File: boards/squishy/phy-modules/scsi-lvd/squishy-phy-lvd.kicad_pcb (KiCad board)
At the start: 6 copper layers, 75 x 55 mm, 22 parts, among them J1 SCSI PHY Mezz, J2 SCSI Connector, U1 M24C02-RMC

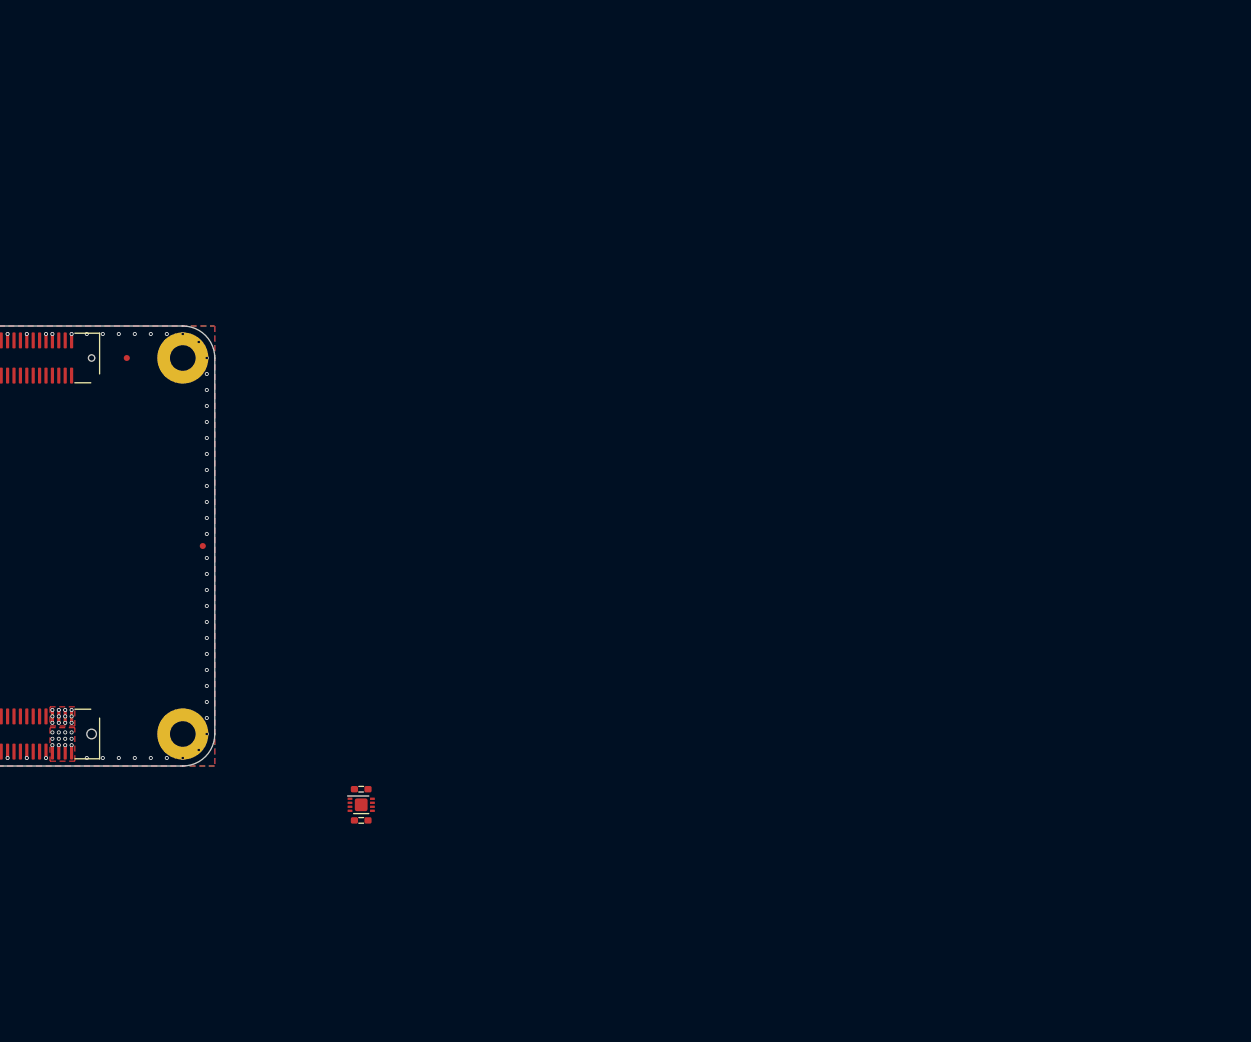
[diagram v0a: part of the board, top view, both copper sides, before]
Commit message: squishy: phy: lvd: Large chunk of work on the LVD phy,
still needs diffsense and termpwr bits implemented and then it can be routed
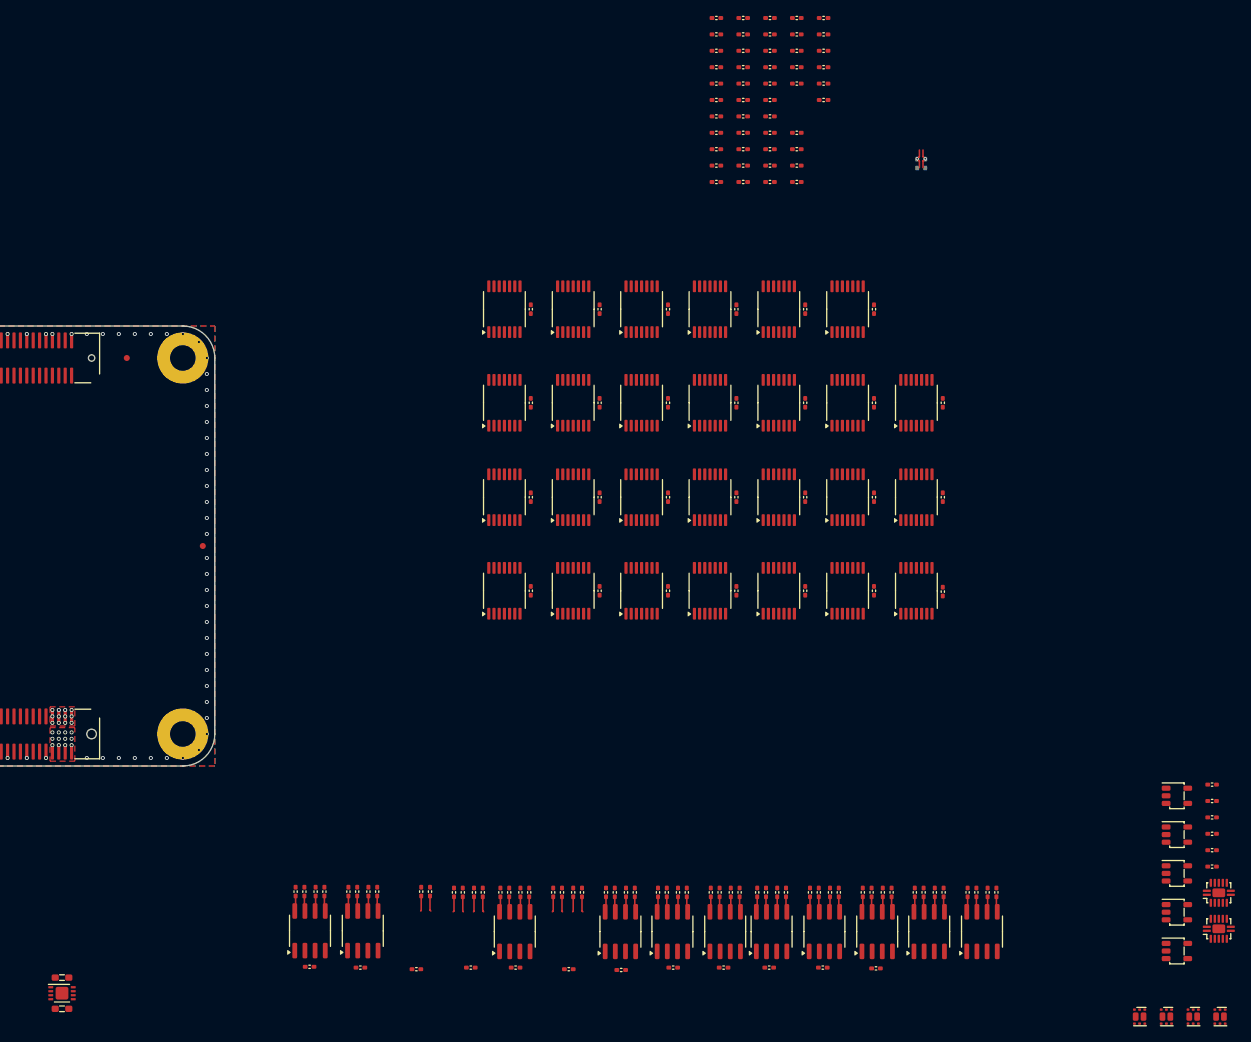
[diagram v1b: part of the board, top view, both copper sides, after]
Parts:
- added C10: 3p, rhais_rcl:C0402, F.Cu at (263.0, 155.8)
- added C100: 1u, rhais_rcl:C0402, F.Cu at (250.2, 82.9)
- added C101: 1u, rhais_rcl:C0402, F.Cu at (258.8, 82.9)
- added C103: 1u, rhais_rcl:C0402, F.Cu at (267.4, 82.9)
- added C106: 1u, rhais_rcl:C0402, F.Cu at (242.3, 165.2)
- added C107: 1u, rhais_rcl:C0402, F.Cu at (248.6, 165.2)
- added C108: 1u, rhais_rcl:C0402, F.Cu at (196.8, 165.1)
- added C109: 1u, rhais_rcl:C0402, F.Cu at (203.2, 165.2)
- added C11: 3p, rhais_rcl:C0402, F.Cu at (259.4, 155.8)
- added C110: 1u, rhais_rcl:C0402, F.Cu at (210.2, 165.4)
- added C111: 1u, rhais_rcl:C0402, F.Cu at (217.0, 165.2)
- added C12: 3p, rhais_rcl:C0402, F.Cu at (260.5, 155.8)
- added C13: 1u, rhais_rcl:C0402, F.Cu at (241.7, 118.1)
- added C14: 1u, rhais_rcl:C0402, F.Cu at (250.2, 118.1)
- added C15: 1u, rhais_rcl:C0402, F.Cu at (261.0, 165.2)
- added C16: 3p, rhais_rcl:C0402, F.Cu at (268.5, 155.8)
- added C17: 3p, rhais_rcl:C0402, F.Cu at (269.6, 155.8)
- added C18: 3p, rhais_rcl:C0402, F.Cu at (266.0, 155.8)
- added C19: 3p, rhais_rcl:C0402, F.Cu at (267.1, 155.8)
- added C2: 3p, rhais_rcl:C0402, F.Cu at (255.3, 155.8)
- added C20: 1u, rhais_rcl:C0402, F.Cu at (258.8, 118.1)
- added C21: 1u, rhais_rcl:C0402, F.Cu at (267.4, 118.1)
- added C22: 1u, rhais_rcl:C0402, F.Cu at (267.6, 165.3)
- added C23: 3p, rhais_rcl:C0402, F.Cu at (275.0, 155.8)
- added C24: 3p, rhais_rcl:C0402, F.Cu at (276.1, 155.8)
- added C25: 3p, rhais_rcl:C0402, F.Cu at (272.5, 155.8)
- added C26: 3p, rhais_rcl:C0402, F.Cu at (273.6, 155.8)
- added C27: 1u, rhais_rcl:C0402, F.Cu at (276.0, 118.2)
- added C28: 1u, rhais_rcl:C0402, F.Cu at (224.5, 106.4)
- added C3: 3p, rhais_rcl:C0402, F.Cu at (256.4, 155.8)
- added C30: 3p, rhais_rcl:C0402, F.Cu at (281.6, 155.8)
- added C31: 3p, rhais_rcl:C0402, F.Cu at (282.7, 155.8)
- added C32: 3p, rhais_rcl:C0402, F.Cu at (279.1, 155.8)
- added C33: 3p, rhais_rcl:C0402, F.Cu at (280.2, 155.8)
- added C34: 1u, rhais_rcl:C0402, F.Cu at (233.1, 106.4)
- added C35: 1u, rhais_rcl:C0402, F.Cu at (241.7, 106.4)
- added C37: 3p, rhais_rcl:C0402, F.Cu at (223.2, 155.8)
- added C38: 3p, rhais_rcl:C0402, F.Cu at (224.3, 155.8)
- added C39: 3p, rhais_rcl:C0402, F.Cu at (220.7, 155.8)
- added C4: 3p, rhais_rcl:C0402, F.Cu at (252.8, 155.8)
- added C40: 3p, rhais_rcl:C0402, F.Cu at (221.8, 155.8)
- added C41: 1u, rhais_rcl:C0402, F.Cu at (250.2, 106.4)
- added C42: 1u, rhais_rcl:C0402, F.Cu at (258.8, 106.4)
- added C43: 1u, rhais_rcl:C0402, F.Cu at (222.6, 165.2)
- added C44: 3p, rhais_rcl:C0402, F.Cu at (229.8, 155.8)
- added C45: 3p, rhais_rcl:C0402, F.Cu at (230.9, 155.8)
- added C46: 3p, rhais_rcl:C0402, F.Cu at (227.3, 155.8)
- added C47: 3p, rhais_rcl:C0402, F.Cu at (228.4, 155.8)
- added C48: 1u, rhais_rcl:C0402, F.Cu at (267.4, 106.4)
- added C49: 1u, rhais_rcl:C0402, F.Cu at (276.0, 106.4)
- added C5: 3p, rhais_rcl:C0402, F.Cu at (253.9, 155.8)
- added C50: 1u, rhais_rcl:C0402, F.Cu at (229.2, 165.4)
- added C51: 3p, rhais_rcl:C0402, F.Cu at (236.4, 155.8)
- added C52: 3p, rhais_rcl:C0402, F.Cu at (237.5, 155.8)
- added C53: 3p, rhais_rcl:C0402, F.Cu at (233.9, 155.8)
- added C54: 3p, rhais_rcl:C0402, F.Cu at (235.0, 155.8)
- added C55: 1u, rhais_rcl:C0402, F.Cu at (224.5, 94.6)
- added C56: 1u, rhais_rcl:C0402, F.Cu at (233.1, 94.6)
- added C57: 1u, rhais_rcl:C0402, F.Cu at (235.8, 165.5)
- added C58: 3p, rhais_rcl:C0402, F.Cu at (242.9, 155.8)
- added C59: 3p, rhais_rcl:C0402, F.Cu at (249.5, 155.8)
- added C6: 1u, rhais_rcl:C0402, F.Cu at (224.5, 118.1)
- added C60: 3p, rhais_rcl:C0402, F.Cu at (197.6, 155.7)
- added C61: 3p, rhais_rcl:C0402, F.Cu at (204.2, 155.7)
- added C62: 3p, rhais_rcl:C0402, F.Cu at (210.8, 155.7)
- added C63: 3p, rhais_rcl:C0402, F.Cu at (217.4, 155.8)
- added C64: 1u, rhais_rcl:C0402, F.Cu at (309.7, 142.3)
- added C65: 1u, rhais_rcl:C0402, F.Cu at (309.7, 144.4)
- added C66: 3p, rhais_rcl:C0402, F.Cu at (244.0, 155.8)
- added C67: 3p, rhais_rcl:C0402, F.Cu at (250.6, 155.8)
- added C68: 3p, rhais_rcl:C0402, F.Cu at (198.7, 155.7)
- added C69: 3p, rhais_rcl:C0402, F.Cu at (205.3, 155.7)
- added C7: 1u, rhais_rcl:C0402, F.Cu at (233.1, 118.1)
- added C70: 3p, rhais_rcl:C0402, F.Cu at (211.9, 155.7)
- added C71: 3p, rhais_rcl:C0402, F.Cu at (218.5, 155.8)
- added C72: 1u, rhais_rcl:C0402, F.Cu at (309.7, 146.4)
- added C73: 1u, rhais_rcl:C0402, F.Cu at (309.7, 148.5)
- added C74: 3p, rhais_rcl:C0402, F.Cu at (240.4, 155.8)
- added C75: 3p, rhais_rcl:C0402, F.Cu at (247.0, 155.8)
- added C76: 3p, rhais_rcl:C0402, F.Cu at (195.1, 155.7)
- added C77: 3p, rhais_rcl:C0402, F.Cu at (201.7, 155.7)
- added C78: 1u, rhais_rcl:C0402, F.Cu at (309.7, 150.5)
- added C79: 3p, rhais_rcl:C0402, F.Cu at (214.9, 155.8)
- added C8: 1u, rhais_rcl:C0402, F.Cu at (254.3, 165.2)
- added C80: 1u, rhais_rcl:C0402, F.Cu at (309.7, 152.6)
- added C82: 3p, rhais_rcl:C0402, F.Cu at (241.5, 155.8)
- added C83: 3p, rhais_rcl:C0402, F.Cu at (248.1, 155.8)
- added C84: 3p, rhais_rcl:C0402, F.Cu at (196.2, 155.7)
- added C85: 3p, rhais_rcl:C0402, F.Cu at (202.8, 155.7)
- added C87: 3p, rhais_rcl:C0402, F.Cu at (216.0, 155.8)
- added C9: 3p, rhais_rcl:C0402, F.Cu at (261.9, 155.8)
- added C90: 1u, rhais_rcl:C0402, F.Cu at (241.7, 94.6)
- added C91: 1u, rhais_rcl:C0402, F.Cu at (250.2, 94.6)
- added C92: 1u, rhais_rcl:C0402, F.Cu at (258.8, 94.6)
- added C93: 1u, rhais_rcl:C0402, F.Cu at (267.4, 94.6)
- added C94: 1u, rhais_rcl:C0402, F.Cu at (276.0, 94.6)
- added C95: 1u, rhais_rcl:C0402, F.Cu at (224.5, 82.9)
- added C98: 1u, rhais_rcl:C0402, F.Cu at (233.1, 82.9)
- added C99: 1u, rhais_rcl:C0402, F.Cu at (241.7, 82.9)
- added Q1: PMDPB58UPE,115, lethalbit-so:SOT1118-3, F.Cu at (300.6, 171.3)
- added Q2: PMDPB58UPE,115, lethalbit-so:SOT1118-3, F.Cu at (303.9, 171.3)
- added Q3: PMDPB58UPE,115, lethalbit-so:SOT1118-3, F.Cu at (307.3, 171.3)
- added Q4: PMDPB58UPE,115, lethalbit-so:SOT1118-3, F.Cu at (310.6, 171.3)
- added R10: 75, rhais_rcl:R0402, F.Cu at (247.7, 62.9)
- added R11: 75, rhais_rcl:R0402, F.Cu at (247.7, 65.0)
- added R12: 75, rhais_rcl:R0402, F.Cu at (247.7, 67.0)
- added R13: 75, rhais_rcl:R0402, F.Cu at (251.1, 46.5)
- added R14: 75, rhais_rcl:R0402, F.Cu at (251.1, 48.5)
- added R15: 75, rhais_rcl:R0402, F.Cu at (251.1, 50.6)
- added R16: 75, rhais_rcl:R0402, F.Cu at (251.1, 52.6)
- added R17: 75, rhais_rcl:R0402, F.Cu at (251.1, 54.7)
- added R18: 75, rhais_rcl:R0402, F.Cu at (251.1, 56.8)
- added R19: 75, rhais_rcl:R0402, F.Cu at (251.1, 58.8)
- added R2: 75, rhais_rcl:R0402, F.Cu at (247.7, 46.5)
- added R20: 75, rhais_rcl:R0402, F.Cu at (251.1, 60.9)
- added R21: 75, rhais_rcl:R0402, F.Cu at (251.1, 62.9)
- added R22: 75, rhais_rcl:R0402, F.Cu at (251.1, 65.0)
- added R23: 75, rhais_rcl:R0402, F.Cu at (251.1, 67.0)
- added R24: 75, rhais_rcl:R0402, F.Cu at (254.4, 46.5)
- added R25: 75, rhais_rcl:R0402, F.Cu at (254.4, 48.5)
- added R26: 75, rhais_rcl:R0402, F.Cu at (254.4, 50.6)
- added R27: 75, rhais_rcl:R0402, F.Cu at (254.4, 52.6)
- added R28: 75, rhais_rcl:R0402, F.Cu at (254.4, 54.7)
- added R29: 75, rhais_rcl:R0402, F.Cu at (254.4, 56.8)
- added R3: 75, rhais_rcl:R0402, F.Cu at (247.7, 48.5)
- added R30: 75, rhais_rcl:R0402, F.Cu at (254.4, 58.8)
- added R31: 75, rhais_rcl:R0402, F.Cu at (254.4, 60.9)
- added R32: 75, rhais_rcl:R0402, F.Cu at (254.4, 62.9)
- added R33: 75, rhais_rcl:R0402, F.Cu at (254.4, 65.0)
- added R34: 75, rhais_rcl:R0402, F.Cu at (254.4, 67.0)
- added R35: 75, rhais_rcl:R0402, F.Cu at (257.8, 46.5)
- added R36: 75, rhais_rcl:R0402, F.Cu at (257.8, 48.5)
- added R37: 75, rhais_rcl:R0402, F.Cu at (257.8, 50.6)
- added R38: 75, rhais_rcl:R0402, F.Cu at (257.8, 52.6)
- added R39: 75, rhais_rcl:R0402, F.Cu at (257.8, 54.7)
- added R4: 75, rhais_rcl:R0402, F.Cu at (247.7, 50.6)
- added R40: 75, rhais_rcl:R0402, B.Cu at (272.8, 64.7)
- added R41: 75, rhais_rcl:R0402, B.Cu at (273.8, 64.7)
- added R42: 75, rhais_rcl:R0402, F.Cu at (257.8, 60.9)
- added R43: 75, rhais_rcl:R0402, F.Cu at (257.8, 62.9)
- added R44: 75, rhais_rcl:R0402, F.Cu at (257.8, 65.0)
- added R45: 75, rhais_rcl:R0402, F.Cu at (257.8, 67.0)
- added R46: 75, rhais_rcl:R0402, F.Cu at (261.1, 46.5)
- added R47: 75, rhais_rcl:R0402, F.Cu at (261.1, 48.5)
- added R48: 75, rhais_rcl:R0402, F.Cu at (261.1, 50.6)
- added R49: 75, rhais_rcl:R0402, F.Cu at (261.1, 52.6)
- added R5: 75, rhais_rcl:R0402, F.Cu at (247.7, 52.6)
- added R50: 75, rhais_rcl:R0402, F.Cu at (261.1, 54.7)
- added R51: 75, rhais_rcl:R0402, F.Cu at (261.1, 56.8)
- added R6: 75, rhais_rcl:R0402, F.Cu at (247.7, 54.7)
- added R7: 75, rhais_rcl:R0402, F.Cu at (247.7, 56.8)
- added R8: 75, rhais_rcl:R0402, F.Cu at (247.7, 58.8)
- added R9: 75, rhais_rcl:R0402, F.Cu at (247.7, 60.9)
- added U10: SN65LVDS180-Q1, Package_SO:TSSOP-14_4.4x5mm_P0.65mm, F.Cu at (264.1, 118.1)
- added U11: SN65LVDS180-Q1, Package_SO:TSSOP-14_4.4x5mm_P0.65mm, F.Cu at (272.7, 118.1)
- added U12: FIN1027A, Package_SO:SOIC-8_3.9x4.9mm_P1.27mm, F.Cu at (274.3, 160.7)
- added U13: SN65LVDS180-Q1, Package_SO:TSSOP-14_4.4x5mm_P0.65mm, F.Cu at (221.2, 106.4)
- added U14: SN65LVDS180-Q1, Package_SO:TSSOP-14_4.4x5mm_P0.65mm, F.Cu at (229.8, 106.4)
- added U15: FIN1027A, Package_SO:SOIC-8_3.9x4.9mm_P1.27mm, F.Cu at (280.9, 160.7)
- added U16: SN65LVDS180-Q1, Package_SO:TSSOP-14_4.4x5mm_P0.65mm, F.Cu at (238.3, 106.4)
- added U17: SN65LVDS180-Q1, Package_SO:TSSOP-14_4.4x5mm_P0.65mm, F.Cu at (246.9, 106.4)
- added U18: FIN1027A, Package_SO:SOIC-8_3.9x4.9mm_P1.27mm, F.Cu at (222.5, 160.7)
- added U19: SN65LVDS180-Q1, Package_SO:TSSOP-14_4.4x5mm_P0.65mm, F.Cu at (255.5, 106.4)
- added U2: SN65LVDS180-Q1, Package_SO:TSSOP-14_4.4x5mm_P0.65mm, F.Cu at (221.2, 118.1)
- added U20: SN65LVDS180-Q1, Package_SO:TSSOP-14_4.4x5mm_P0.65mm, F.Cu at (264.1, 106.4)
- added U22: SN65LVDS180-Q1, Package_SO:TSSOP-14_4.4x5mm_P0.65mm, F.Cu at (272.7, 106.4)
- added U23: SN65LVDS180-Q1, Package_SO:TSSOP-14_4.4x5mm_P0.65mm, F.Cu at (221.2, 94.6)
- added U24: FIN1027A, Package_SO:SOIC-8_3.9x4.9mm_P1.27mm, F.Cu at (235.7, 160.7)
- added U25: SN65LVDS180-Q1, Package_SO:TSSOP-14_4.4x5mm_P0.65mm, F.Cu at (229.8, 94.6)
- added U26: SN65LVDS180-Q1, Package_SO:TSSOP-14_4.4x5mm_P0.65mm, F.Cu at (238.3, 94.6)
- added U27: SN65LVDS180-Q1, Package_SO:TSSOP-14_4.4x5mm_P0.65mm, F.Cu at (246.9, 94.6)
- added U28: SN65LVDS180-Q1, Package_SO:TSSOP-14_4.4x5mm_P0.65mm, F.Cu at (255.5, 94.6)
- added U29: SN65LVDS180-Q1, Package_SO:TSSOP-14_4.4x5mm_P0.65mm, F.Cu at (264.1, 94.6)
- added U3: FIN1027A, Package_SO:SOIC-8_3.9x4.9mm_P1.27mm, F.Cu at (254.6, 160.7)
- added U30: SN65LVDS180-Q1, Package_SO:TSSOP-14_4.4x5mm_P0.65mm, F.Cu at (272.7, 94.6)
- added U31: SN65LVDS180-Q1, Package_SO:TSSOP-14_4.4x5mm_P0.65mm, F.Cu at (221.2, 82.9)
- added U32: ~, rhais_package-qfn:DHVQFN-14-1EP_2.5x3mm_P0.5mm_EP1x1.5mm, F.Cu at (310.5, 155.8)
- added U33: ~, rhais_package-qfn:DHVQFN-14-1EP_2.5x3mm_P0.5mm_EP1x1.5mm, F.Cu at (310.5, 160.3)
- added U34: FIN1027A, Package_SO:SOIC-8_3.9x4.9mm_P1.27mm, F.Cu at (242.2, 160.7)
- added U35: FIN1027A, Package_SO:SOIC-8_3.9x4.9mm_P1.27mm, F.Cu at (248.8, 160.7)
- added U36: FIN1027A, Package_SO:SOIC-8_3.9x4.9mm_P1.27mm, F.Cu at (196.9, 160.6)
- added U37: FIN1027A, Package_SO:SOIC-8_3.9x4.9mm_P1.27mm, F.Cu at (203.5, 160.6)
- added U4: SN65LVDS180-Q1, Package_SO:TSSOP-14_4.4x5mm_P0.65mm, F.Cu at (229.8, 118.1)
- added U40: ~, rhais_package-smd:SOT-23-5, F.Cu at (305.3, 143.7)
- added U41: ~, rhais_package-smd:SOT-23-5, F.Cu at (305.3, 148.6)
- added U42: SN65LVDS180-Q1, Package_SO:TSSOP-14_4.4x5mm_P0.65mm, F.Cu at (229.8, 82.9)
- added U43: SN65LVDS180-Q1, Package_SO:TSSOP-14_4.4x5mm_P0.65mm, F.Cu at (238.3, 82.9)
- added U44: SN65LVDS180-Q1, Package_SO:TSSOP-14_4.4x5mm_P0.65mm, F.Cu at (246.9, 82.9)
- added U45: SN65LVDS180-Q1, Package_SO:TSSOP-14_4.4x5mm_P0.65mm, F.Cu at (255.5, 82.9)
- added U46: ~, rhais_package-smd:SOT-23-5, F.Cu at (305.3, 153.4)
- added U47: SN65LVDS180-Q1, Package_SO:TSSOP-14_4.4x5mm_P0.65mm, F.Cu at (264.1, 82.9)
- added U48: ~, rhais_package-smd:SOT-23-5, F.Cu at (305.3, 158.3)
- added U49: ~, rhais_package-smd:SOT-23-5, F.Cu at (305.3, 163.1)
- added U5: SN65LVDS180-Q1, Package_SO:TSSOP-14_4.4x5mm_P0.65mm, F.Cu at (238.3, 118.1)
- added U6: FIN1027A, Package_SO:SOIC-8_3.9x4.9mm_P1.27mm, F.Cu at (261.2, 160.7)
- added U7: SN65LVDS180-Q1, Package_SO:TSSOP-14_4.4x5mm_P0.65mm, F.Cu at (246.9, 118.1)
- added U8: SN65LVDS180-Q1, Package_SO:TSSOP-14_4.4x5mm_P0.65mm, F.Cu at (255.5, 118.1)
- added U9: FIN1027A, Package_SO:SOIC-8_3.9x4.9mm_P1.27mm, F.Cu at (267.8, 160.7)
- moved U1 44.2 mm to (165.9, 168.4)
- moved C1 44.2 mm to (165.9, 170.3)
- moved R1 44.2 mm to (165.9, 166.4)
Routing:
- net /CON.RST-: track 0.00 -> 2.43 mm, vias 0 -> 1
- net /CON.RST+: track 0.00 -> 2.43 mm, vias 0 -> 1
- net Net-(C79-Pad1): track 0.00 -> 1.92 mm
- net Net-(C74-Pad1): track 0.00 -> 1.92 mm
- net Net-(C68-Pad1): track 0.00 -> 1.92 mm
- net Net-(C67-Pad1): track 0.00 -> 1.92 mm
- net Net-(C53-Pad1): track 0.00 -> 1.92 mm
- net Net-(C46-Pad1): track 0.00 -> 1.92 mm
- net Net-(C4-Pad1): track 0.00 -> 1.92 mm
- net Net-(C32-Pad1): track 0.00 -> 1.92 mm
- net Net-(C31-Pad1): track 0.00 -> 1.92 mm
- net Net-(C3-Pad1): track 0.00 -> 1.92 mm
- net Net-(C25-Pad1): track 0.00 -> 1.92 mm
- net Net-(C18-Pad1): track 0.00 -> 1.92 mm
- net Net-(C10-Pad1): track 0.00 -> 1.92 mm
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
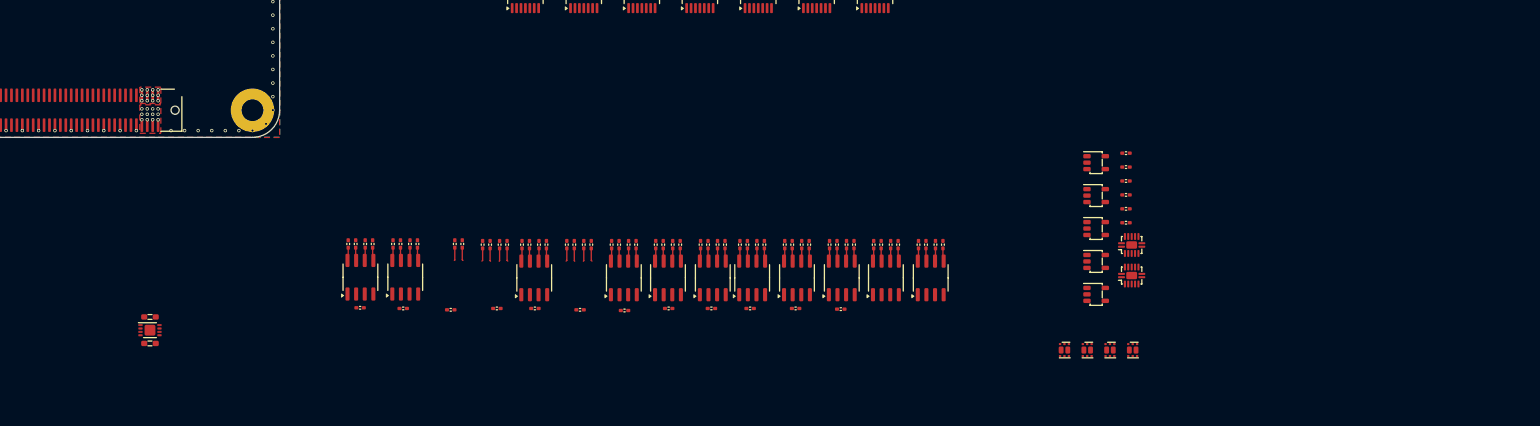
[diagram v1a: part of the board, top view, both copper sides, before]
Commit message: squishy: phy: lvd: updated the PCB with the mostly finished schematic bits.
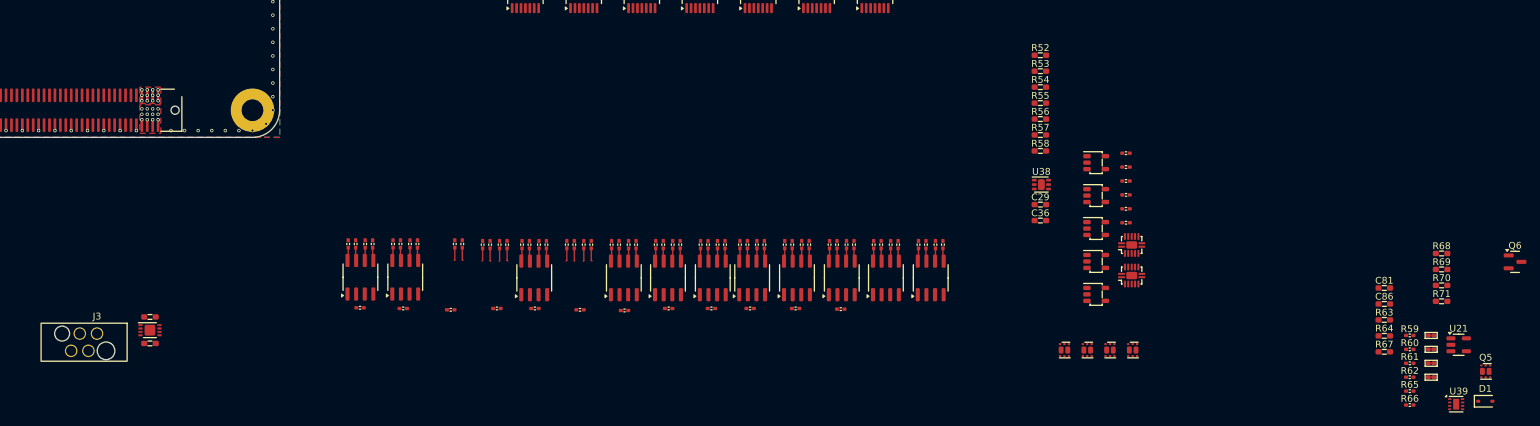
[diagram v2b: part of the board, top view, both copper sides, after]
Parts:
- added C29: 1u, rhais_rcl:C0603, F.Cu at (297.1, 149.9)
- added C36: 1u, rhais_rcl:C0603, F.Cu at (297.1, 152.2)
- added C81: 100n, rhais_rcl:C0603, F.Cu at (347.7, 162.2)
- added C86: 100n, rhais_rcl:C0603, F.Cu at (347.7, 164.5)
- added D1: Vz=2V @ 2%, Diode_SMD:D_SOD-323, F.Cu at (362.6, 178.9)
- added J3: Conn_01x04, pkl_connectors_wuerth:490107670412-d, F.Cu at (158.1, 168.9)
- added JP1: PWR_JMPR, pkl_jumpers:J_NC_0402_30, F.Cu at (354.6, 169.2)
- added JP2: PWR_JMPR, pkl_jumpers:J_NC_0402_30, F.Cu at (354.6, 171.2)
- added JP3: PWR_JMPR, pkl_jumpers:J_NC_0402_30, F.Cu at (354.6, 173.3)
- added JP4: PWR_JMPR, pkl_jumpers:J_NC_0402_30, F.Cu at (354.6, 175.3)
- added Q5: PMDPB58UPE,115, lethalbit-so:SOT1118-3, F.Cu at (362.7, 174.5)
- added Q6: DMN65D8L-7, Package_TO_SOT_SMD:SOT-23, F.Cu at (367.0, 158.3)
- added R52: 10k, rhais_rcl:R0603, F.Cu at (297.1, 127.9)
- added R53: 10k, rhais_rcl:R0603, F.Cu at (297.1, 130.2)
- added R54: 10k, rhais_rcl:R0603, F.Cu at (297.1, 132.6)
- added R55: 10k, rhais_rcl:R0603, F.Cu at (297.1, 134.9)
- added R56: 10k, rhais_rcl:R0603, F.Cu at (297.1, 137.3)
- added R57: 10k, rhais_rcl:R0603, F.Cu at (297.1, 139.7)
- added R58: 10k, rhais_rcl:R0603, F.Cu at (297.1, 142.0)
- added R59: 300, rhais_rcl:R0402, F.Cu at (351.5, 169.2)
- added R60: 220k, rhais_rcl:R0402, F.Cu at (351.5, 171.2)
- added R61: 220k, rhais_rcl:R0402, F.Cu at (351.5, 173.3)
- added R62: 100k, rhais_rcl:R0402, F.Cu at (351.5, 175.3)
- added R63: 10k, rhais_rcl:R0603, F.Cu at (347.7, 166.9)
- added R64: 10k, rhais_rcl:R0603, F.Cu at (347.7, 169.2)
- added R65: 100k, rhais_rcl:R0402, F.Cu at (351.5, 177.4)
- added R66: 175k, rhais_rcl:R0402, F.Cu at (351.5, 179.4)
- added R67: 10k, rhais_rcl:R0603, F.Cu at (347.7, 171.6)
- added R68: 10k, rhais_rcl:R0603, F.Cu at (356.1, 157.1)
- added R69: 10k, rhais_rcl:R0603, F.Cu at (356.1, 159.4)
- added R70: 10k, rhais_rcl:R0603, F.Cu at (356.1, 161.8)
- added R71: 10k, rhais_rcl:R0603, F.Cu at (356.1, 164.2)
- added U21: LM321, Package_TO_SOT_SMD:SOT-23-5, F.Cu at (358.7, 170.6)
- added U38: TLV75512PDRV, rhais_package-qfn:WSON-6-1EP_2x2mm_P0.65mm_EP1x1.6mm, F.Cu at (297.2, 146.9)
- added U39: LM2903, Package_SON:WSON-8-1EP_2x2mm_P0.5mm_EP0.9x1.6mm, F.Cu at (358.3, 179.3)
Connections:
- net /Termination/1v2 renamed /INT_TERMPWR
- J2 pad 3: unconnected-(J2-Pin_3-Pad3) -> +3V3

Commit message: squishy: phy: lvd: Started re-working the LVD PHY
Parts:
- removed R10, R11, R12, R13, R14, R15, R16, R17, R18, R19, R2, R20, R21, R22, R23, R24, R25, R26, R27, R28, R29, R3, R30, R31, R32, R33, R34, R35, R36, R37, R38, R39, R4, R40, R41, R42, R43, R44, R45, R46, R47, R48, R49, R5, R50, R51, R6, R7, R8, R9: 75, rhais_rcl:R0402
- added C88: 4u7, rhais_rcl:C0402, F.Cu at (140.7, 60.3)
- added C89: 4u7, rhais_rcl:C0402, F.Cu at (170.8, 68.2)
- added R74: 100k, rhais_rcl:R0402, F.Cu at (167.0, 72.0)
- added R75: 100k, rhais_rcl:R0402, F.Cu at (167.0, 71.0)
- added U50: UCC5640PW24, Package_SO:TSSOP-24_4.4x7.8mm_P0.65mm, F.Cu at (147.5, 61.5)
- added U51: UCC5640PW24, Package_SO:TSSOP-24_4.4x7.8mm_P0.65mm, F.Cu at (136.0, 61.5)
- C29, C36: value 1u -> 4u7; footprint rhais_rcl:C0603 -> rhais_rcl:C0402
- U38: value TLV75512PDRV -> UCC5640PW24; footprint rhais_package-qfn:WSON-6-1EP_2x2mm_P0.65mm_EP1x1.6mm -> Package_SO:TSSOP-24_4.4x7.8mm_P0.65mm
- moved C36 171.6 mm to (152.2, 60.3), turned to 90 degrees
- moved U38 162.5 mm to (159.0, 61.5), turned to -90 degrees
- moved C29 160.7 mm to (163.7, 60.3), turned to 90 degrees
- moved U15 145.8 mm to (150.0, 225.0)
- moved C24 139.9 mm to (151.8, 220.0)
- moved C23 139.9 mm to (150.8, 220.0)
- moved U12 133.3 mm to (157.5, 225.0)
- moved C17 123.3 mm to (164.3, 220.0)
- moved C16 123.3 mm to (163.2, 220.0)
- moved U9 121.3 mm to (165.0, 225.0)
- moved C59 119.9 mm to (148.2, 220.0)
- moved C67 119.9 mm to (149.3, 220.0)
- moved C32 113.3 mm to (185.8, 220.1)
- moved C33 113.3 mm to (186.8, 220.1)
- moved C30 113.3 mm to (188.2, 220.0)
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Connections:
- C29 pad 1: /INT_TERMPWR -> GND
- C29 pad 2: GND -> Net-(U38A-REG)
- C36 pad 1: +5V -> GND
- C36 pad 2: GND -> Net-(U50A-REG)
- U38 pad 1: /INT_TERMPWR -> Net-(U38A-REG)
- U38 pad 2: unconnected-(U38-NC-Pad2) -> /CON.DB12+
- U38 pad 3: GND -> /CON.DB12-
- U38 pad 4: /PHY.LS_CTRL5 -> /CON.DB14+
- U38 pad 5: unconnected-(U38-NC-Pad5) -> /CON.DB14-
- U38 pad 6: +5V -> /CON.DP1+
- U38 pad 7: GND -> /CON.DP1-
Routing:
- net /CON.RST-: track 2.43 -> 0.00 mm, vias 1 -> 0
- net /CON.RST+: track 2.43 -> 0.00 mm, vias 1 -> 0
- net Net-(U51A-REG): track 0.00 -> 1.97 mm
- net Net-(U50A-REG): track 0.00 -> 1.97 mm
- net Net-(U38A-REG): track 0.00 -> 1.97 mm
- net Net-(C79-Pad1): track 1.92 -> 0.00 mm
- net Net-(C74-Pad1): track 1.92 -> 0.00 mm
- net Net-(C68-Pad1): track 1.92 -> 0.00 mm
- net Net-(C67-Pad1): track 1.92 -> 0.00 mm
- net Net-(C53-Pad1): track 1.92 -> 0.00 mm
- net Net-(C46-Pad1): track 1.92 -> 0.00 mm
- net Net-(C4-Pad1): track 1.92 -> 0.00 mm
- net Net-(C32-Pad1): track 1.92 -> 0.00 mm
- net Net-(C31-Pad1): track 1.92 -> 0.00 mm
- net Net-(C3-Pad1): track 1.92 -> 0.00 mm
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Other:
- board size 75 x 55 mm -> 75 x 92.5 mm
